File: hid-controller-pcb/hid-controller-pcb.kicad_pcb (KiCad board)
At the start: 2 copper layers, 2 parts, among them J1 10118194-0011LF, U1 STM32F103C8Tx

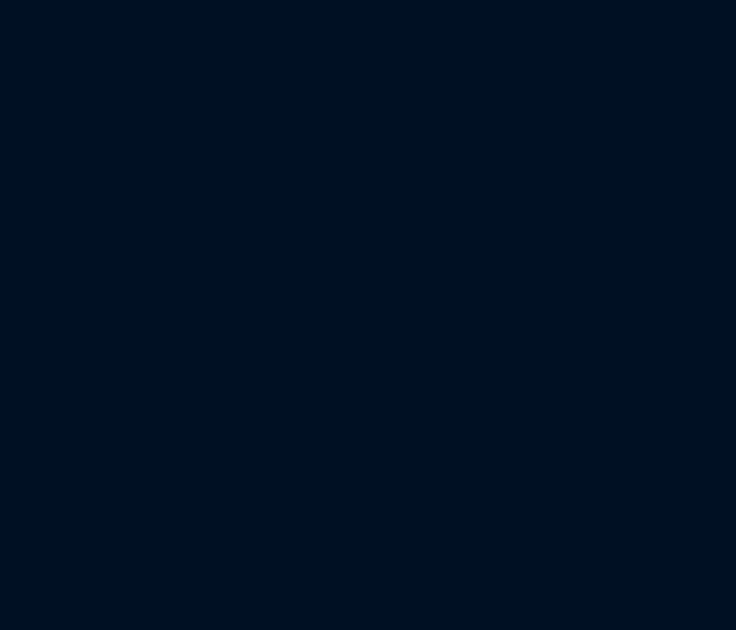
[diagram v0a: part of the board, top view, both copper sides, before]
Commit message: HSE / LSE finished, onto analog
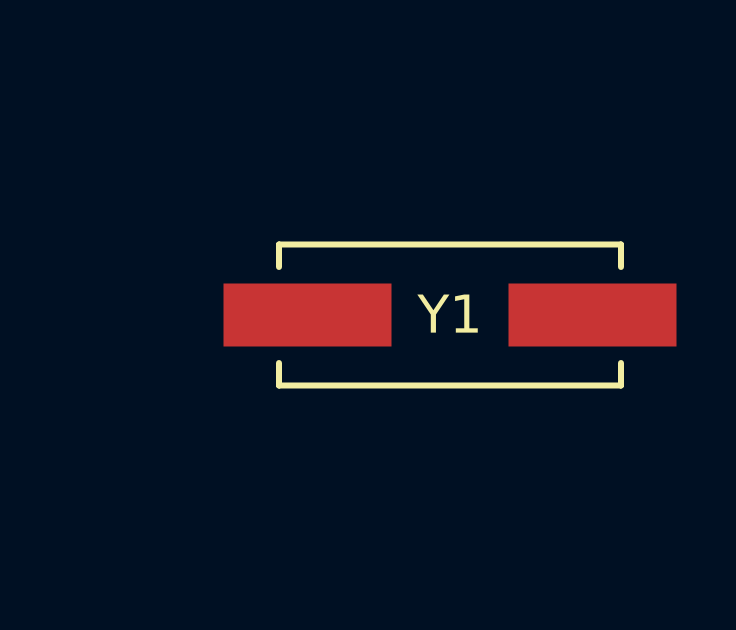
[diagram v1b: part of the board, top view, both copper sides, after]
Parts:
- added Y1: 8MHz, lib:ABLS-8.000MHZ-B4-T, F.Cu at (143.6, 86.2)
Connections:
- U1 pad 20: unconnected-(U1-PB2-Pad20) -> BOOT1
- U1 pad 44: unconnected-(U1-BOOT0-Pad44) -> BOOT0
- U1 pad 5: unconnected-(U1-PD0-Pad5) -> OSC_IN
- U1 pad 6: unconnected-(U1-PD1-Pad6) -> OSC_OUT

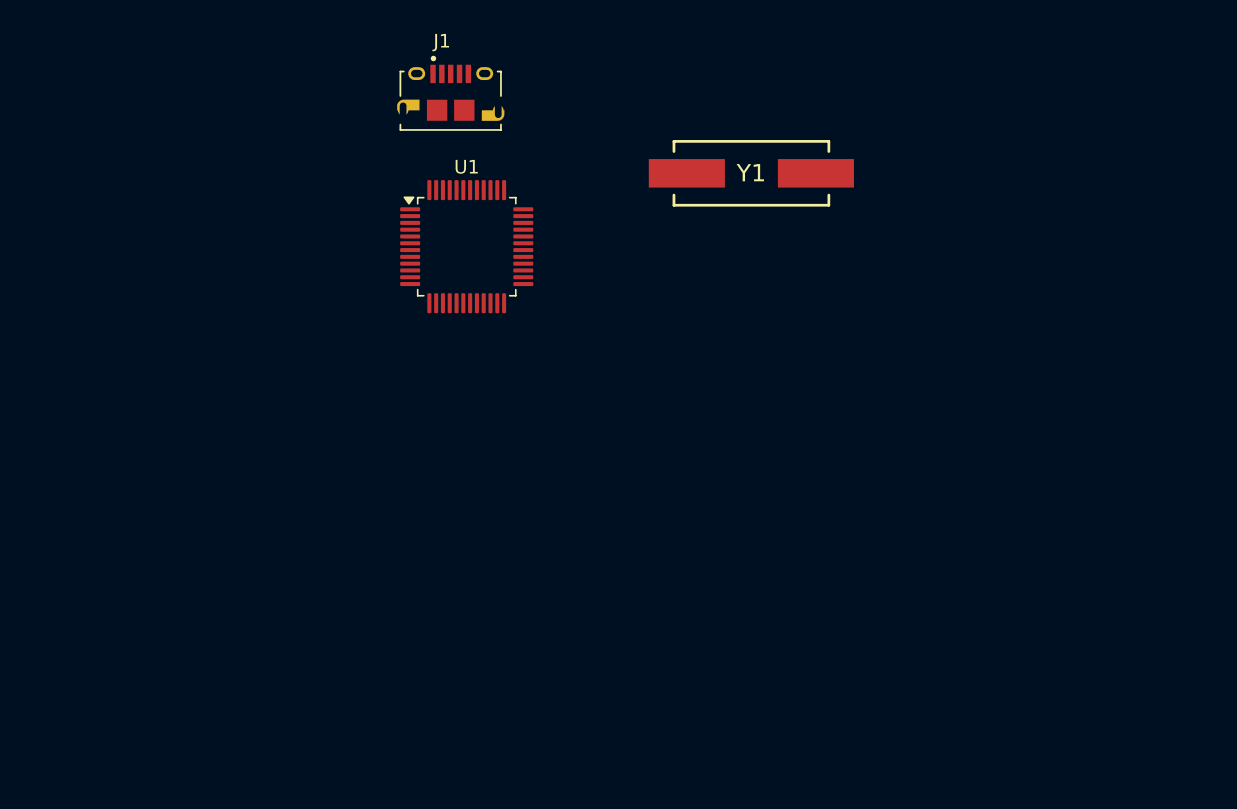
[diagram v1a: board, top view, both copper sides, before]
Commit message: Added joysticks / buttons, made STM32CubeMX project
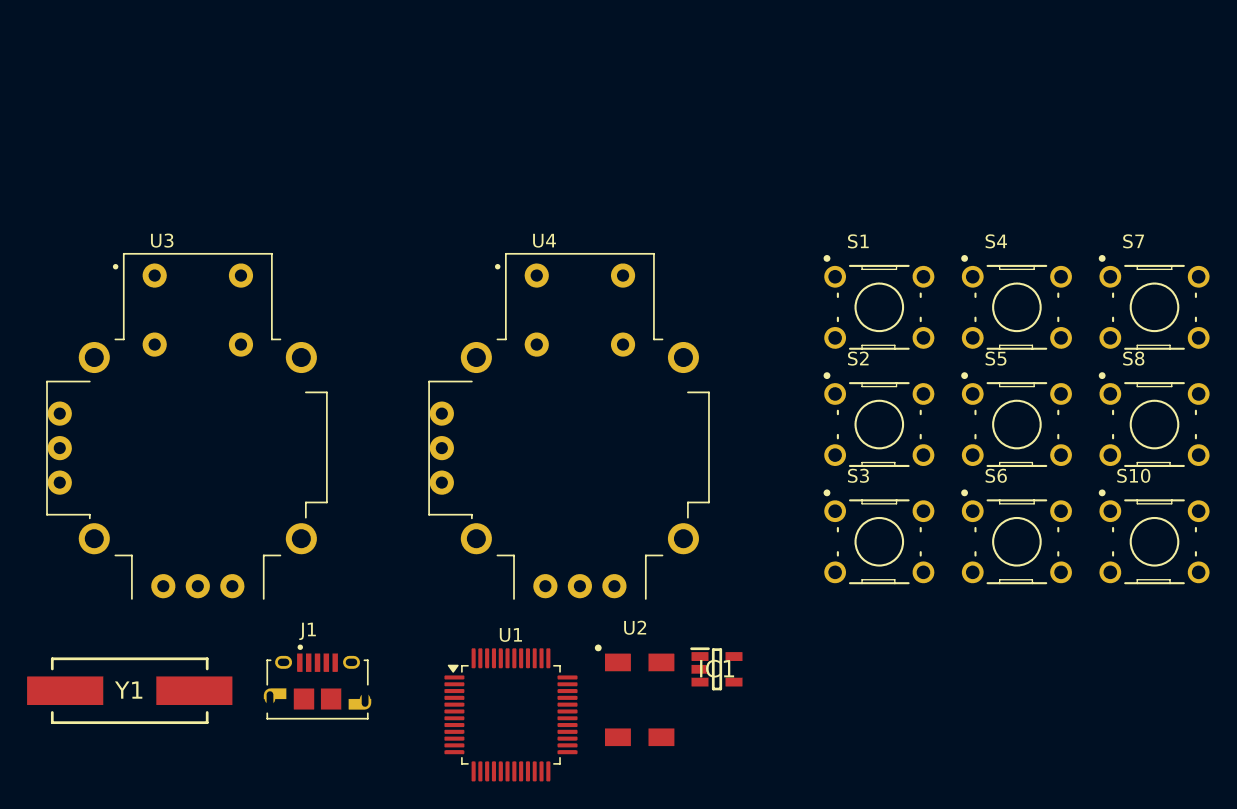
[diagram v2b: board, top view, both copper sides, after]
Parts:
- added IC1: RT9080-33GJ5, lib:RT9080-33GJ5, F.Cu at (141.0, 122.7)
- added S1: B3F-1000, lib:SW_B3F-1000, F.Cu at (153.0, 96.1)
- added S10: B3F-1000, lib:SW_B3F-1000, F.Cu at (173.2, 113.3)
- added S2: B3F-1000, lib:SW_B3F-1000, F.Cu at (153.0, 104.7)
- added S3: B3F-1000, lib:SW_B3F-1000, F.Cu at (153.0, 113.3)
- added S4: B3F-1000, lib:SW_B3F-1000, F.Cu at (163.1, 96.1)
- added S5: B3F-1000, lib:SW_B3F-1000, F.Cu at (163.1, 104.7)
- added S6: B3F-1000, lib:SW_B3F-1000, F.Cu at (163.1, 113.3)
- added S7: B3F-1000, lib:SW_B3F-1000, F.Cu at (173.2, 96.1)
- added S8: B3F-1000, lib:SW_B3F-1000, F.Cu at (173.2, 104.7)
- added U2: 32.768KHz, lib:CM200C32768DZCT, F.Cu at (135.3, 125.0)
- added U3: COM-09032, lib:XDCR_COM-09032, F.Cu at (102.8, 106.4)
- added U4: COM-09032, lib:XDCR_COM-09032, F.Cu at (130.9, 106.4)
- moved Y1 59.5 mm to (97.8, 124.3)
- moved J1 44.4 mm to (111.6, 124.9)
- moved U1 34.6 mm to (125.9, 126.1)
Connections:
- J1 pad 4: GND -> BOOT1
- J1 pad 5: GND -> BOOT1
- J1 pad S1: GND -> BOOT1
- J1 pad S2: GND -> BOOT1
- J1 pad S3: GND -> BOOT1
- J1 pad S4: GND -> BOOT1
- J1 pad S5: GND -> BOOT1
- J1 pad S6: GND -> BOOT1
- U1 pad 11: unconnected-(U1-PA1-Pad11) -> AN_A1
- U1 pad 12: unconnected-(U1-PA2-Pad12) -> AN_B1
- U1 pad 14: unconnected-(U1-PA4-Pad14) -> AN_A2
- U1 pad 15: unconnected-(U1-PA5-Pad15) -> AN_B2
- U1 pad 21: unconnected-(U1-PB10-Pad21) -> AN_SEL1
- U1 pad 22: unconnected-(U1-PB11-Pad22) -> AN_SEL2
- U1 pad 23: GND -> BOOT1
- U1 pad 24: unconnected-(U1-VDD-Pad24) -> Net-(U1-VDDA)
- U1 pad 3: unconnected-(U1-PC14-Pad3) -> OSC32_IN
- U1 pad 35: GND -> BOOT1
- U1 pad 36: unconnected-(U1-VDD-Pad36) -> Net-(U1-VDDA)
- U1 pad 4: unconnected-(U1-PC15-Pad4) -> OSC32_OUT
- U1 pad 47: GND -> BOOT1
- U1 pad 48: unconnected-(U1-VDD-Pad48) -> Net-(U1-VDDA)
- U1 pad 8: GND -> BOOT1
- U1 pad 9: unconnected-(U1-VDDA-Pad9) -> Net-(U1-VDDA)

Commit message: schematic finished? now onto layout
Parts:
- added C1: 4.7uF, Capacitor_SMD:C_0603_1608Metric, F.Cu at (114.9, 100.6)
- added C2: 26pF, Capacitor_SMD:C_0603_1608Metric, F.Cu at (114.9, 103.1)
- added C3: 26pF, Capacitor_SMD:C_0603_1608Metric, F.Cu at (114.9, 105.7)
- added C4: 8pF, Capacitor_SMD:C_0603_1608Metric, F.Cu at (114.9, 108.2)
- added C5: 8pF, Capacitor_SMD:C_0603_1608Metric, F.Cu at (114.9, 110.7)
- added C6: 0.1uF, Capacitor_SMD:C_0603_1608Metric, F.Cu at (114.9, 113.2)
- added C7: 0.1uF, Capacitor_SMD:C_0603_1608Metric, F.Cu at (118.9, 100.6)
- added C8: 2.2uF, Capacitor_SMD:C_0603_1608Metric, F.Cu at (118.9, 103.1)
- added D1: 3.4V, lib:SMFA2005CA, F.Cu at (134.7, 94.0)
- added D2: 6V, lib:DIODE_VESD05A1B-HD1-GS08_VIS, F.Cu at (90.1, 118.6)
- added J2: Jumper, Connector_PinHeader_2.54mm:PinHeader_1x03_P2.54mm_Vertical, F.Cu at (131.2, 113.0)
- added R1: 22R, Resistor_SMD:R_0603_1608Metric, F.Cu at (118.9, 105.7)
- added R10: 20kR, Resistor_SMD:R_0603_1608Metric, F.Cu at (122.9, 113.2)
- added R11: 20kR, Resistor_SMD:R_0603_1608Metric, F.Cu at (126.9, 100.6)
- added R12: 20kR, Resistor_SMD:R_0603_1608Metric, F.Cu at (126.9, 103.1)
- added R13: 20kR, Resistor_SMD:R_0603_1608Metric, F.Cu at (126.9, 105.7)
- added R14: 20kR, Resistor_SMD:R_0603_1608Metric, F.Cu at (126.9, 108.2)
- added R15: 20kR, Resistor_SMD:R_0603_1608Metric, F.Cu at (126.9, 110.7)
- added R16: 20kR, Resistor_SMD:R_0603_1608Metric, F.Cu at (126.9, 113.2)
- added R2: 22R, Resistor_SMD:R_0603_1608Metric, F.Cu at (118.9, 108.2)
- added R3: 1.5kR, Resistor_SMD:R_0603_1608Metric, F.Cu at (118.9, 110.7)
- added R4: 1.5kR, Resistor_SMD:R_0603_1608Metric, F.Cu at (118.9, 113.2)
- added R5: 68kR, Resistor_SMD:R_0603_1608Metric, F.Cu at (122.9, 100.6)
- added R6: 13kR, Resistor_SMD:R_0603_1608Metric, F.Cu at (122.9, 103.1)
- added R7: 1.5kR, Resistor_SMD:R_0603_1608Metric, F.Cu at (122.9, 105.7)
- added R8: 1.5kR, Resistor_SMD:R_0603_1608Metric, F.Cu at (122.9, 108.2)
- added R9: 20kR, Resistor_SMD:R_0603_1608Metric, F.Cu at (122.9, 110.7)
- moved S1 65.4 mm to (87.6, 96.1)
- moved S10 65.4 mm to (107.8, 113.4)
- moved S2 65.4 mm to (87.6, 104.8)
- moved S3 65.4 mm to (87.6, 113.4)
- moved S7 65.4 mm to (107.8, 96.1)
- moved S8 65.4 mm to (107.8, 104.8)
- moved S4 65.4 mm to (97.7, 96.1)
- moved S5 65.4 mm to (97.7, 104.8)
- moved S6 65.4 mm to (97.7, 113.4)
- moved IC1 55.9 mm to (85.2, 119.8)
- moved Y1 37.6 mm to (122.0, 95.5)
- moved U3 29.5 mm to (96.6, 77.6)
- moved U4 29.5 mm to (124.7, 77.6)
- moved U1 22.7 mm to (134.6, 105.1)
- moved U2 9.85 mm to (137.3, 115.3)
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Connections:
- U1 pad 16: unconnected-(U1-PA6-Pad16) -> DPAD_1
- U1 pad 17: unconnected-(U1-PA7-Pad17) -> DPAD_2
- U1 pad 29: unconnected-(U1-PA8-Pad29) -> DPAD_3
- U1 pad 30: unconnected-(U1-PA9-Pad30) -> DPAD_4
- U1 pad 34: unconnected-(U1-PA13-Pad34) -> SWDIO
- U1 pad 37: unconnected-(U1-PA14-Pad37) -> SWCLK
- U1 pad 42: unconnected-(U1-PB6-Pad42) -> BTN_1
- U1 pad 43: unconnected-(U1-PB7-Pad43) -> BTN_2
- U1 pad 45: unconnected-(U1-PB8-Pad45) -> BTN_3
- U1 pad 46: unconnected-(U1-PB9-Pad46) -> BTN_4

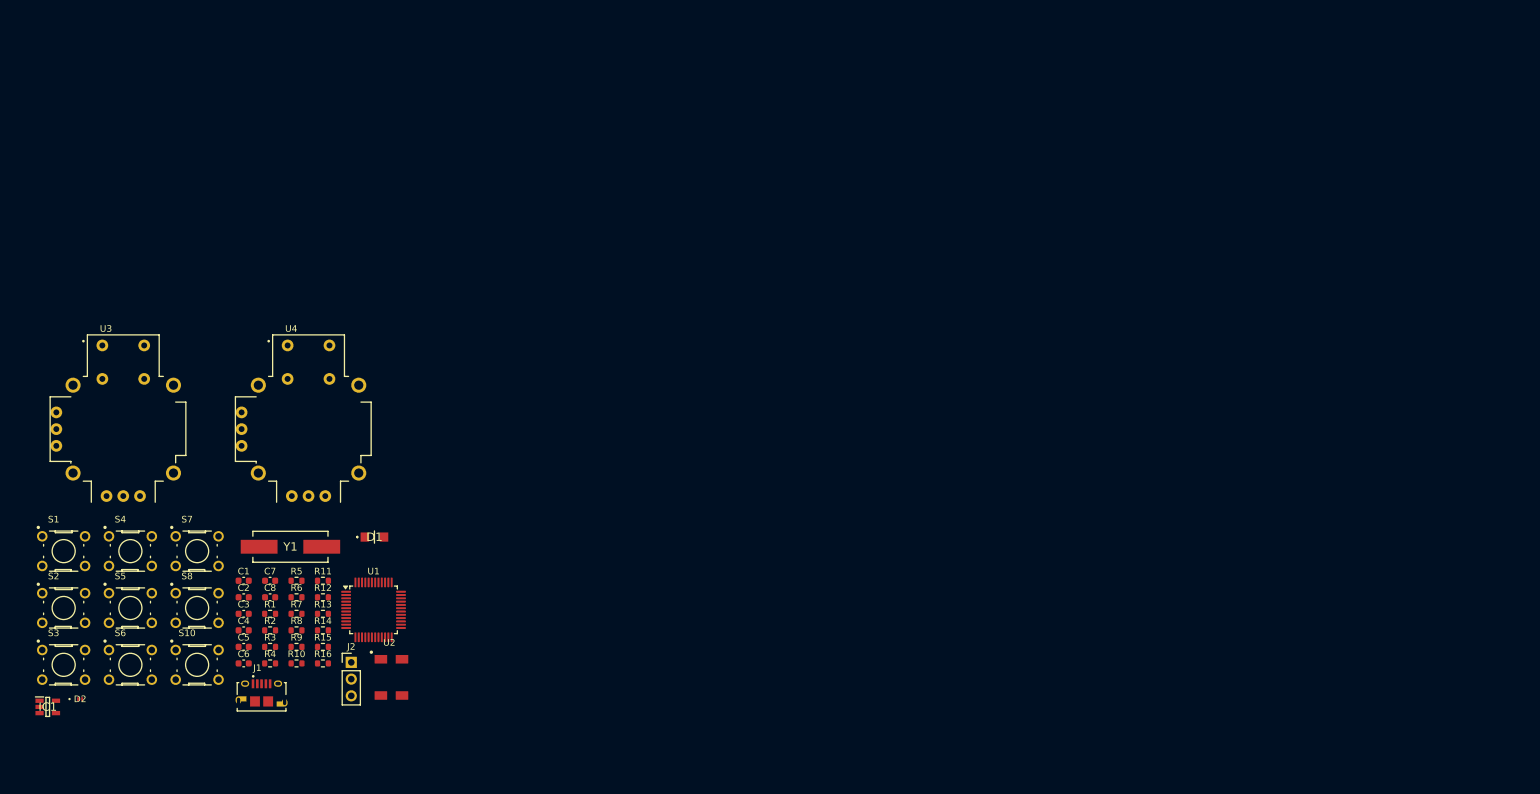
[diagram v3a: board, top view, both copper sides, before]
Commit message: gruelling layout work on the LSE / HSE oscillators
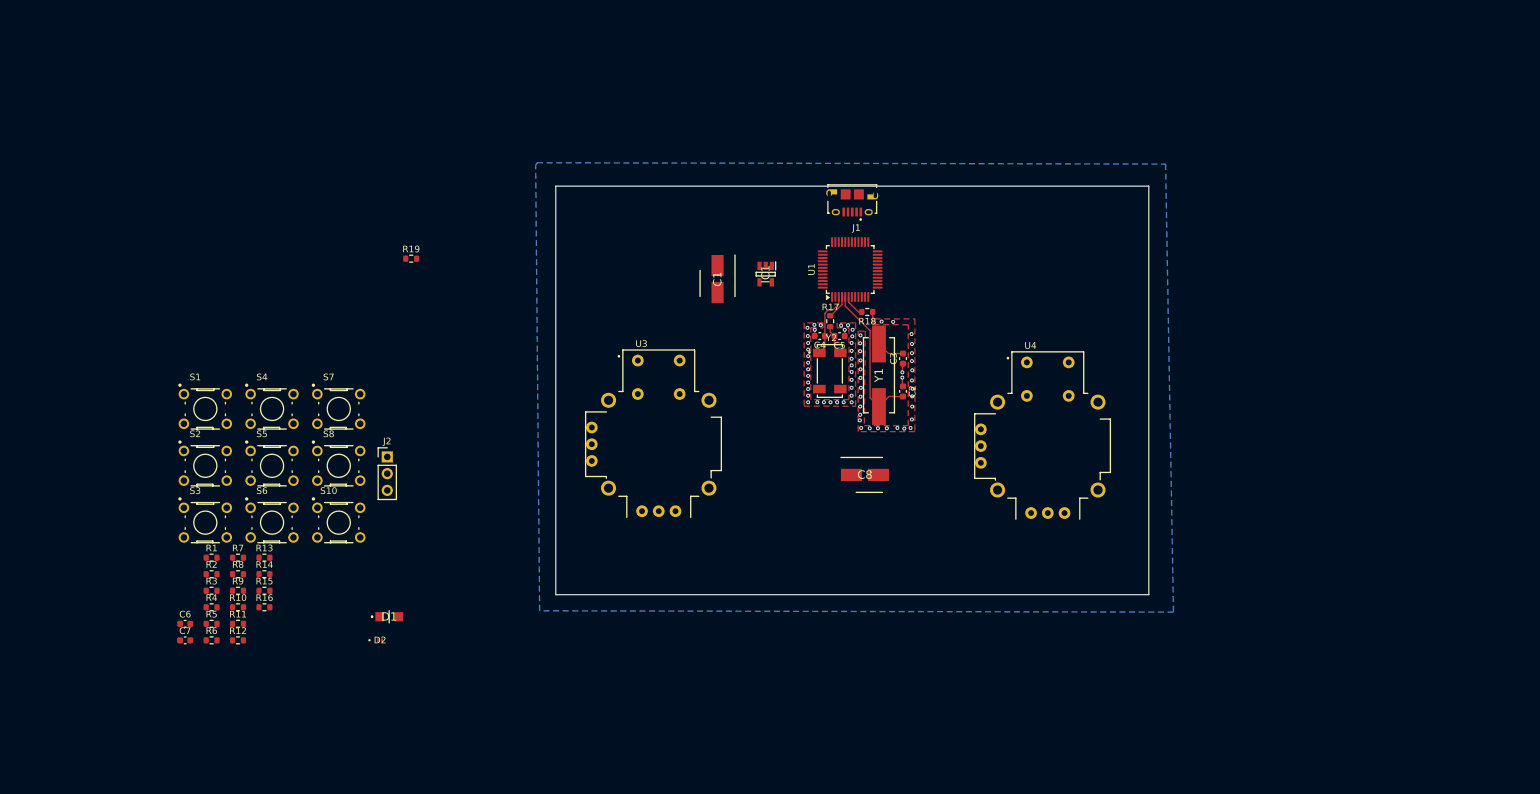
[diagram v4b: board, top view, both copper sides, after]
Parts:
- removed U2: 32.768KHz, lib:CM200C32768DZCT
- added R17: 0R, Resistor_SMD:R_0603_1608Metric, F.Cu at (203.9, 61.2)
- added R18: 663R, Resistor_SMD:R_0603_1608Metric, F.Cu at (209.5, 59.9)
- added R19: 0R, Resistor_SMD:R_0603_1608Metric, F.Cu at (140.3, 51.8)
- added Y2: 32.768KHz, lib:XTAL_ABS25-32.768KHZ-6-T, F.Cu at (203.8, 68.8)
- C1: value 4.7uF -> 10uF; footprint Capacitor_SMD:C_0603_1608Metric -> lib:CAPAE530X550N
- C2, C3: value 26pF -> 30pF
- C4, C5: value 8pF -> 6pF
- C8: value 2.2uF -> 10uF; footprint Capacitor_SMD:C_0603_1608Metric -> lib:CAPAE530X550N
- moved IC1 127.2 mm to (194.1, 54.1), turned to -90 degrees
- moved J1 118.1 mm to (207.2, 42.0), turned to 180 degrees
- moved U4 112.2 mm to (236.9, 80.2)
- moved C3 107.3 mm to (214.9, 66.9), turned to 90 degrees
- moved C2 104.8 mm to (214.9, 71.9), turned to -90 degrees
- moved C5 102.0 mm to (205.3, 63.5), turned to 180 degrees
- moved C4 98.2 mm to (202.3, 63.5)
- moved Y1 93.0 mm to (211.3, 69.5), turned to -90 degrees
- moved C8 92.2 mm to (209.2, 84.6)
- moved U1 88.9 mm to (206.9, 53.4), turned to 90 degrees
- moved C1 85.3 mm to (186.8, 54.9), turned to -90 degrees
- moved U3 81.3 mm to (177.9, 79.9)
- moved D2 46.4 mm to (135.6, 109.7)
- moved J2 31.7 mm to (136.7, 81.8)
- moved S1 30.5 mm to (109.1, 74.6)
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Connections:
- C1 pad 2: BOOT1 -> GND
- C2 pad 1: BOOT1 -> GND
- C3 pad 1: BOOT1 -> GND
- C3 pad 2: OSC_OUT -> Net-(C3-Pad2)
- C4 pad 1: BOOT1 -> GND
- C5 pad 1: BOOT1 -> GND
- C5 pad 2: OSC32_OUT -> Net-(C5-Pad2)
- C6 pad 2: BOOT1 -> GND
- C7 pad 2: BOOT1 -> GND
- C8 pad 2: BOOT1 -> GND
- D1 pad 2: BOOT1 -> GND
- D2 pad 2: BOOT1 -> GND
- IC1 pad 2: BOOT1 -> GND
- J1 pad 4: BOOT1 -> GND
- J1 pad 5: BOOT1 -> GND
- J1 pad S1: BOOT1 -> GND
- J1 pad S2: BOOT1 -> GND
- J1 pad S3: BOOT1 -> GND
- J1 pad S4: BOOT1 -> GND
- J1 pad S5: BOOT1 -> GND
- J1 pad S6: BOOT1 -> GND
- J2 pad 1: BOOT1 -> GND
- R10 pad 2: BOOT1 -> GND
- R11 pad 2: BOOT1 -> GND
- R12 pad 2: BOOT1 -> GND
- R13 pad 2: BOOT1 -> GND
- R14 pad 2: BOOT1 -> GND
- R15 pad 2: BOOT1 -> GND
- R16 pad 2: BOOT1 -> GND
- R6 pad 2: BOOT1 -> GND
- R9 pad 2: BOOT1 -> GND
- S10 pad 3: BOOT1 -> GND
- S10 pad 4: BOOT1 -> GND
- U1 pad 23: BOOT1 -> GND
- U1 pad 35: BOOT1 -> GND
- U1 pad 47: BOOT1 -> GND
- U1 pad 8: BOOT1 -> GND
- U3 pad B2A: BOOT1 -> GND
- U3 pad H3: BOOT1 -> GND
- U3 pad S1: BOOT1 -> GND
- U3 pad S2: BOOT1 -> GND
- U3 pad S3: BOOT1 -> GND
- U3 pad S4: BOOT1 -> GND
- U3 pad V3: BOOT1 -> GND
- U4 pad B2A: BOOT1 -> GND
- U4 pad H3: BOOT1 -> GND
- U4 pad S1: BOOT1 -> GND
- U4 pad S2: BOOT1 -> GND
- U4 pad S3: BOOT1 -> GND
- U4 pad S4: BOOT1 -> GND
- U4 pad V3: BOOT1 -> GND
- Y1 pad 1: OSC_OUT -> Net-(C3-Pad2)
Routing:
- net OSC_IN: track 0.00 -> 23.0 mm
- net OSC32_IN: track 0.00 -> 10.1 mm
- net Net-(C3-Pad2): track 0.00 -> 9.49 mm
- net Net-(C5-Pad2): track 0.00 -> 4.62 mm
- net GND: track 0.00 -> 4.61 mm, vias 0 -> 66
- net OSC32_OUT: track 0.00 -> 3.65 mm
- net OSC_OUT: track 0.00 -> 3.45 mm
- added copper zone on B.Cu, net GND
- added copper zone on F.Cu, net GND
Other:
- board outline added: 90 x 62 mm

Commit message: working ADC reading, troubleshooting USB enumeration issues on pc
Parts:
- added C10: 10uF, lib:CAPAE530X550N, F.Cu at (106.9, 66.1)
- added C11: 10uF, lib:CAPAE530X550N, F.Cu at (106.9, 73.6)
- added C12: 0.1uF, Capacitor_SMD:C_0603_1608Metric, F.Cu at (113.6, 56.0)
- added C13: 0.1uF, Capacitor_SMD:C_0603_1608Metric, F.Cu at (113.6, 58.5)
- added C14: 0.1uF, Capacitor_SMD:C_0603_1608Metric, F.Cu at (113.6, 61.0)
- added C9: 10uF, lib:CAPAE530X550N, F.Cu at (106.9, 58.5)
- moved S6 147.0 mm to (260.2, 50.5), turned to 90 degrees
- moved S5 133.6 mm to (250.5, 58.8)
- moved S8 128.1 mm to (250.5, 41.8)
- moved S7 113.8 mm to (240.5, 50.5), turned to -90 degrees
- moved S1 67.9 mm to (169.0, 42.8)
- moved S3 67.6 mm to (168.8, 60.0)
- moved S4 63.6 mm to (178.5, 51.5), turned to 90 degrees
- moved S2 59.7 mm to (160.0, 52.0), turned to 90 degrees
- moved S10 50.4 mm to (84.0, 69.8)
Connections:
- U1 pad 1: unconnected-(U1-VBAT-Pad1) -> +3V3
- U1 pad 24: Net-(U1-VDDA) -> +3V3
- U1 pad 36: Net-(U1-VDDA) -> +3V3
- U1 pad 48: Net-(U1-VDDA) -> +3V3
- U1 pad 9: Net-(U1-VDDA) -> +3V3
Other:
- board size 90 x 62 mm -> 120.2 x 80.5 mm

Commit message: .
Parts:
- added R20: 20kR, Resistor_SMD:R_0603_1608Metric, F.Cu at (307.9, 77.5)
- added R21: 20kR, Resistor_SMD:R_0603_1608Metric, F.Cu at (307.9, 80.0)
- added R22: 20kR, Resistor_SMD:R_0603_1608Metric, F.Cu at (307.9, 82.5)
- added R23: 20kR, Resistor_SMD:R_0603_1608Metric, F.Cu at (307.9, 85.0)
- added R24: 20kR, Resistor_SMD:R_0603_1608Metric, F.Cu at (307.9, 87.5)
- added R25: 20kR, Resistor_SMD:R_0603_1608Metric, F.Cu at (307.9, 90.1)
- added S11: B3F-1000, lib:SW_B3F-1000, F.Cu at (300.8, 89.4)
- added S12: B3F-1000, lib:SW_B3F-1000, F.Cu at (195.2, 54.5)
- added S13: B3F-1000, lib:SW_B3F-1000, F.Cu at (218.5, 53.8)
- added S14: B3F-1000, lib:SW_B3F-1000, F.Cu at (300.8, 115.3)
- added S15: B3F-1000, lib:SW_B3F-1000, F.Cu at (300.8, 123.9)
- added S9: B3F-1000, lib:SW_B3F-1000, F.Cu at (229.5, 50.2)
- R1, R2: footprint Resistor_SMD:R_0603_1608Metric -> Resistor_SMD:R_0805_2012Metric_Pad1.20x1.40mm_HandSolder
- moved IC1 9.60 mm to (193.9, 44.5)
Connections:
- U1 pad 25: unconnected-(U1-PB12-Pad25) -> BTN_SHR
- U1 pad 26: unconnected-(U1-PB13-Pad26) -> BTN_STR
- U1 pad 27: unconnected-(U1-PB14-Pad27) -> BTN_LB
- U1 pad 28: unconnected-(U1-PB15-Pad28) -> BTN_RB
- U1 pad 31: unconnected-(U1-PA10-Pad31) -> BTN_RT
- U1 pad 41: unconnected-(U1-PB5-Pad41) -> BTN_LT
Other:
- board size 120.2 x 80.5 mm -> 120.2 x 66.8 mm
